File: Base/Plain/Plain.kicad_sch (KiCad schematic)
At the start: 17 parts, among them J1 Barrel_Jack_Switch, J2 AudioJack2_Ground, J3 AudioJack2_Ground, J4 Conn_01x04_Pin, Q1 40V

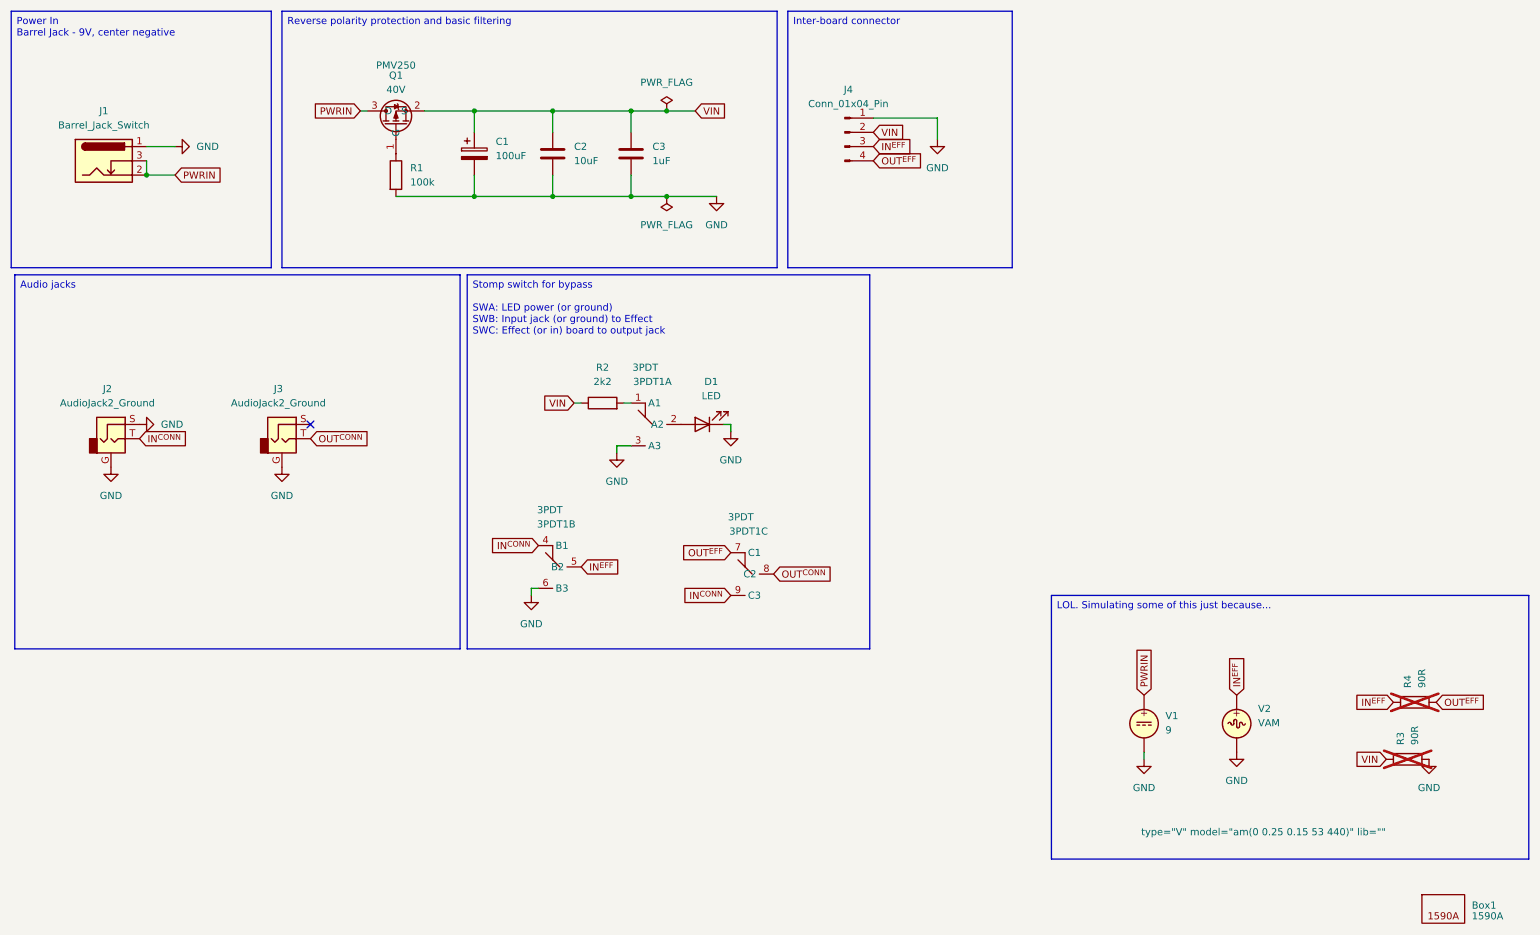
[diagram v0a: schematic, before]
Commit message: First revisions from gen3 testing...
It turns out that while the single connector was sufficient, it is also
mechanically annoyingly less robust than the two separate pin headers we
used to have.

So even though we don't need the extra pins, just split it up into
"power" and a "signal" connectors again.  The placement behind the
output jack was good, so just put the power jack behind the input one
instead.

That ends up making routing nicer with the power trace going down where
it needs to be for the LED anyway, so it's a win-win.  Much nicer than
the old board.  And with the extra pins and the position right next to
the LED, lets just make the base board LED voltage available as an
"active" signal in case anybody ever wants it.

Also, just move the DC blocking capacitor and the anti-pop resistor to
ground to the base board.  Any effects board needs to do that, so it's
one less thing to worry about.  Also add back the low pass RF filter.

With the connector change, this obviously makes the new boards
incompatible, but it's not like I have any legacy boards except for the
test-boards.

On the effect board side, this does the layout changes, but also fixes
the Octaver board that was half-arsed and hadn't done proper bias
voltage calculations.  This basically just reuses them from the boost
board.

Plus use a JFET input on for the Octaver, and while at it make it also
just split the phase the natural way.  Both simpler and more balanced.

So maybe the Octaver works now.

And by "works", I obviously don't mean "sounds good".

Signed-off-by: Linus Torvalds <torvalds@linux-foundation.org>
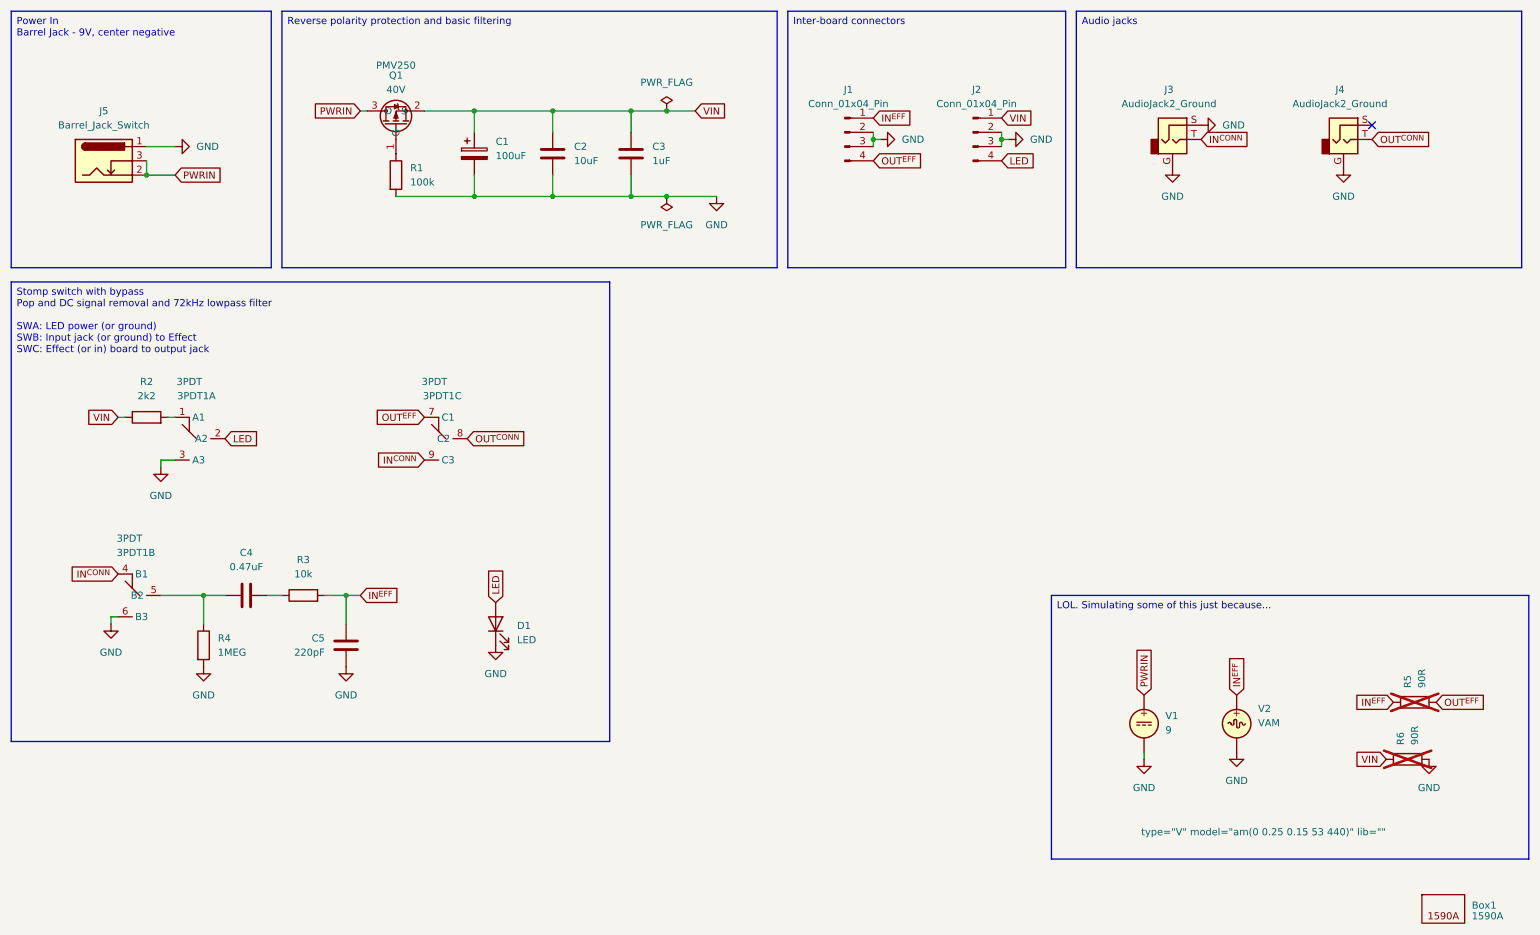
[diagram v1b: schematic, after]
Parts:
- added C4: 0.47uF, Capacitor_SMD:C_1206_3216Metric, symbol Device:C
- added C5: 220pF, Capacitor_SMD:C_0805_2012Metric_Pad1.18x1.45mm_HandSolder, symbol Device:C
- added J2: Conn_01x04_Pin, Connector_PinSocket_2.54mm:PinSocket_1x04_P2.54mm_Vertical, symbol Connector:Conn_01x04_Pin
- added R3: 10k, Resistor_SMD:R_0805_2012Metric_Pad1.20x1.40mm_HandSolder, symbol Device:R
- added R4: 1MEG, Resistor_SMD:R_0805_2012Metric, symbol Device:R
- renumbered J4 to J1, J2 to J3, J3 to J4, J1 to J5, R4 to R5, R3 to R6
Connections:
- net GND: now also J1.2 (Pin_2), J1.3 (Pin_3), C5.2, J2.2 (Pin_2), J2.3 (Pin_3), R4.2; no longer J1.1 (Pin_1)
- net IN^{EFF}: now also J1.1 (Pin_1), C5.1, R3.2; no longer 3PDT1.5 (B2), J1.3 (Pin_3)
- net VIN: now also J2.1 (Pin_1); no longer J1.2 (Pin_2)
- net LED: now reaches 3PDT1.2 (A2), D1.2 (A)
- net LED: now also J2.4 (Pin_4)
- new net: 3PDT1.5 (B2), C4.1, R4.1
- new net: C4.2, R3.1
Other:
- moved on the sheet: 3PDT1A, 3PDT1B, 3PDT1C, D1, J3, J4, R2

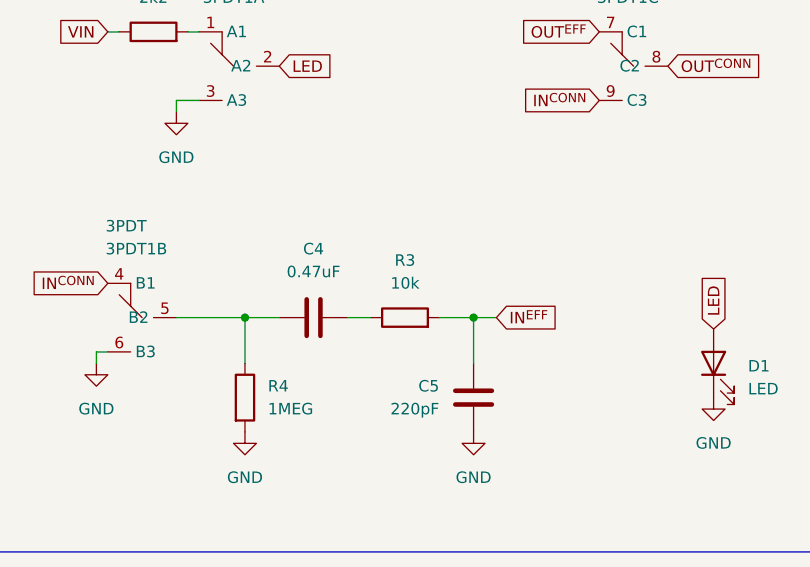
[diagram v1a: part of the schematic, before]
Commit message: Update the plain base to have a 1k RF resistor
That's what the text on the silkscreen said, but I had tested with a 10k
resistor (for a 72kHz low pass filter).  But I think it's safer to
really only filter out RF (3dB at 723kHz), so make it actually match the
text.

Signed-off-by: Linus Torvalds <torvalds@linux-foundation.org>
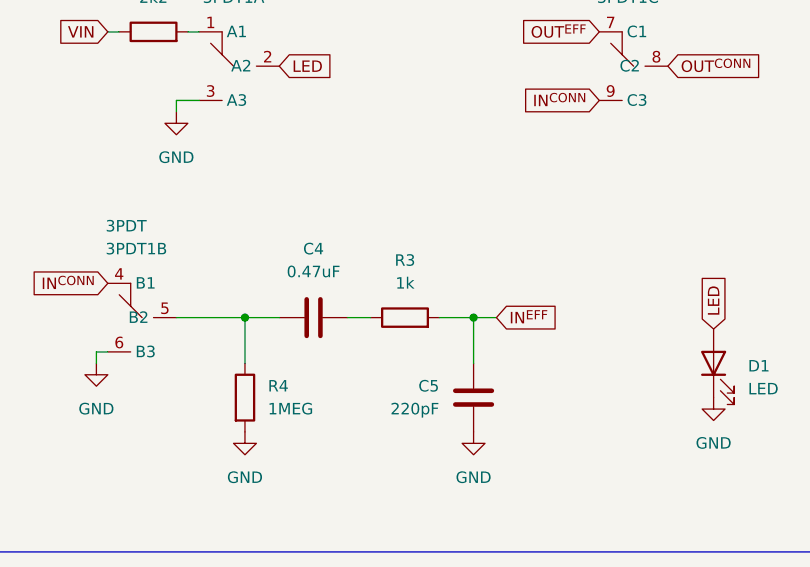
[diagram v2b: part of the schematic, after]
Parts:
- R3: value 10k -> 1k
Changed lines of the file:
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@@
 			)
 		)
-		(property "Value" "10k"
+		(property "Value" "1k"
 			(at 66.04 114.3 90)
 			(effects
